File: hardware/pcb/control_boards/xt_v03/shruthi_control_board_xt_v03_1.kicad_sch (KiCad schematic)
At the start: 29 parts, among them IC1 24LC512, IC10 ATMEGA644p, J1 CV, J2 POWER, J3 M03PTH, J4 POWER, Q1 20MHz, U1 AVRISP, X1 MIDI, X2 MIDI

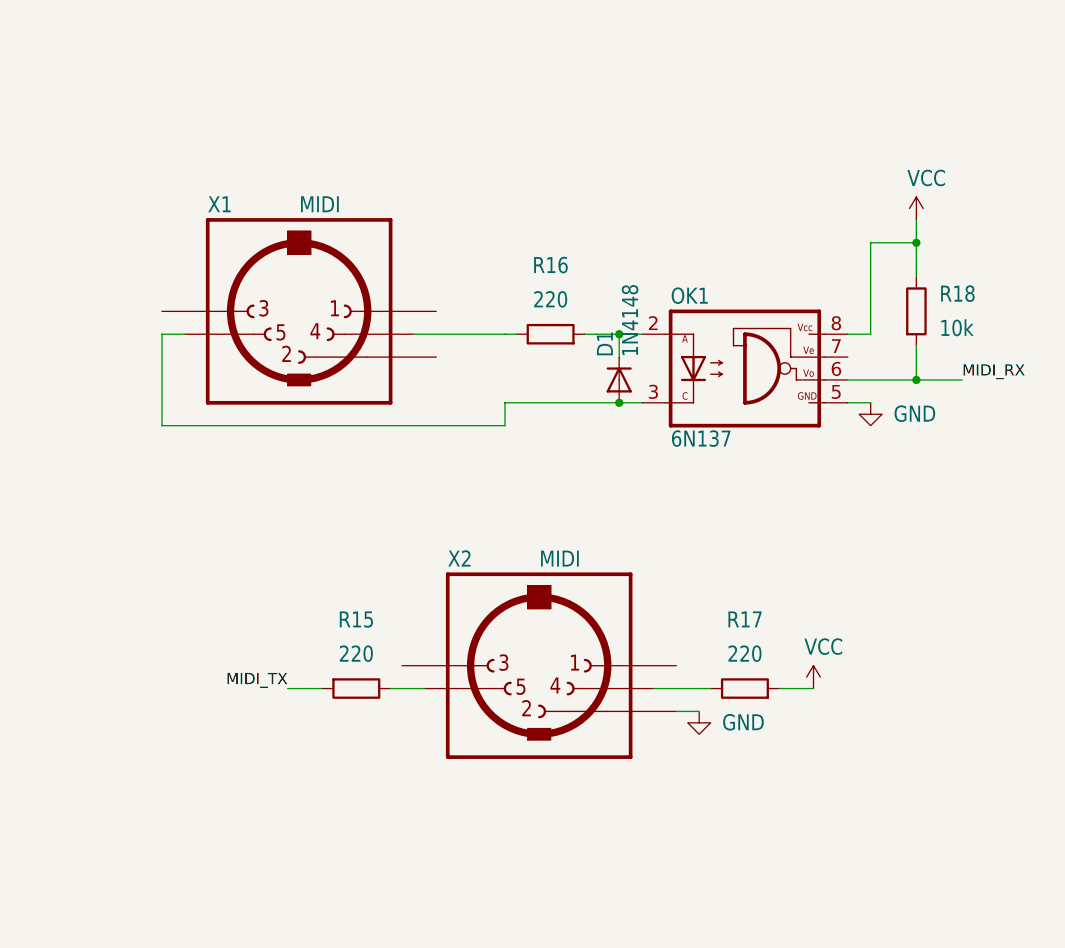
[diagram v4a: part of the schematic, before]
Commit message: update MIDI circuitry to use kicad symbols
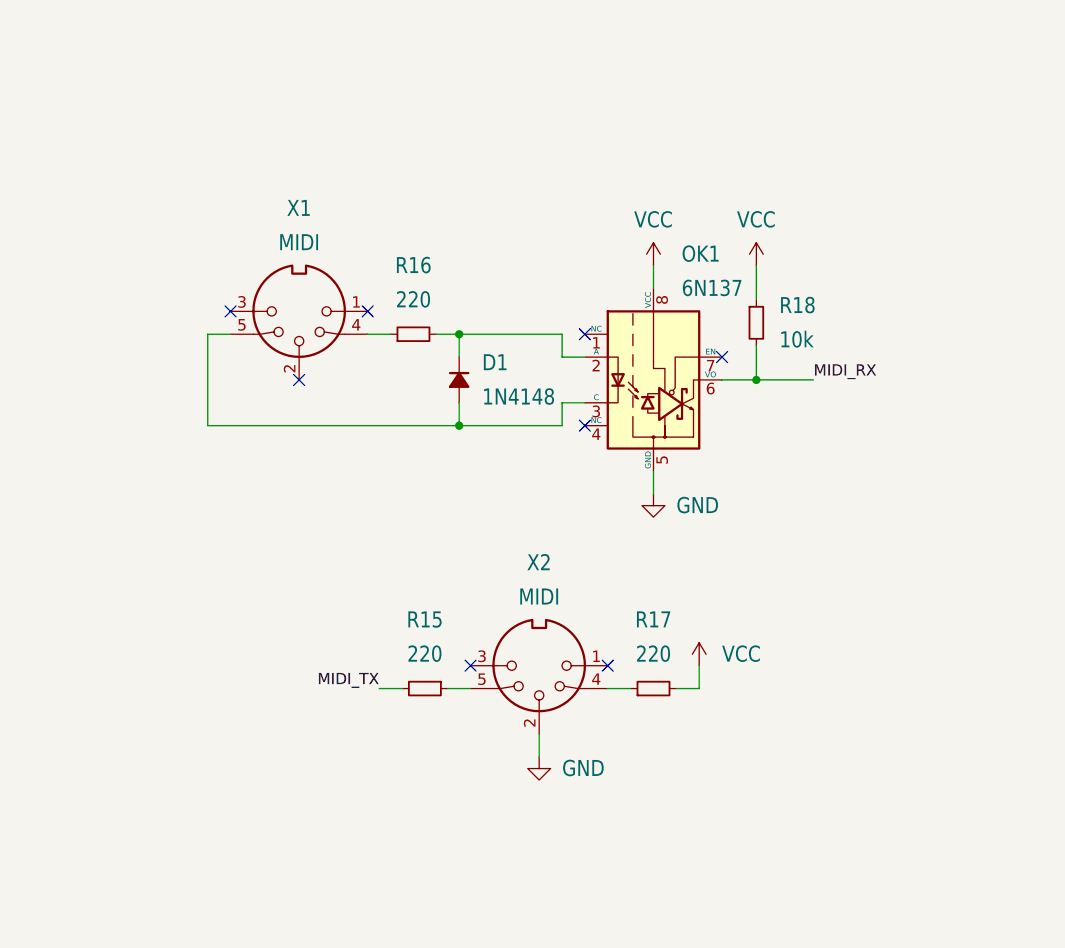
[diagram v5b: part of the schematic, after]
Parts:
- D1: symbol shruthi_control_board_xt_v03-eagle-import:DIODE-D-5 -> Device:D_Small_Filled
- OK1: footprint shruthi_control_board_xt_v03:DIL08 -> Package_DIP:DIP-8_W7.62mm; symbol shruthi_control_board_xt_v03-eagle-import:6N137 -> Isolator:6N137
- R15, R16, R17, R18: symbol Device:R -> Device:R_Small
- X1, X2: symbol shruthi_control_board_xt_v03-eagle-import:MAB5SH -> Connector:DIN-5_180degree
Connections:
- net at OK1.2 (A), R16.2: now also D1.1 (K); no longer D1.C
- net at OK1.3 (C), X1.5: now also D1.2 (A); no longer D1.A
- no-connect marks 0 -> 8
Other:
- moved on the sheet: R15, R16, R17, R18

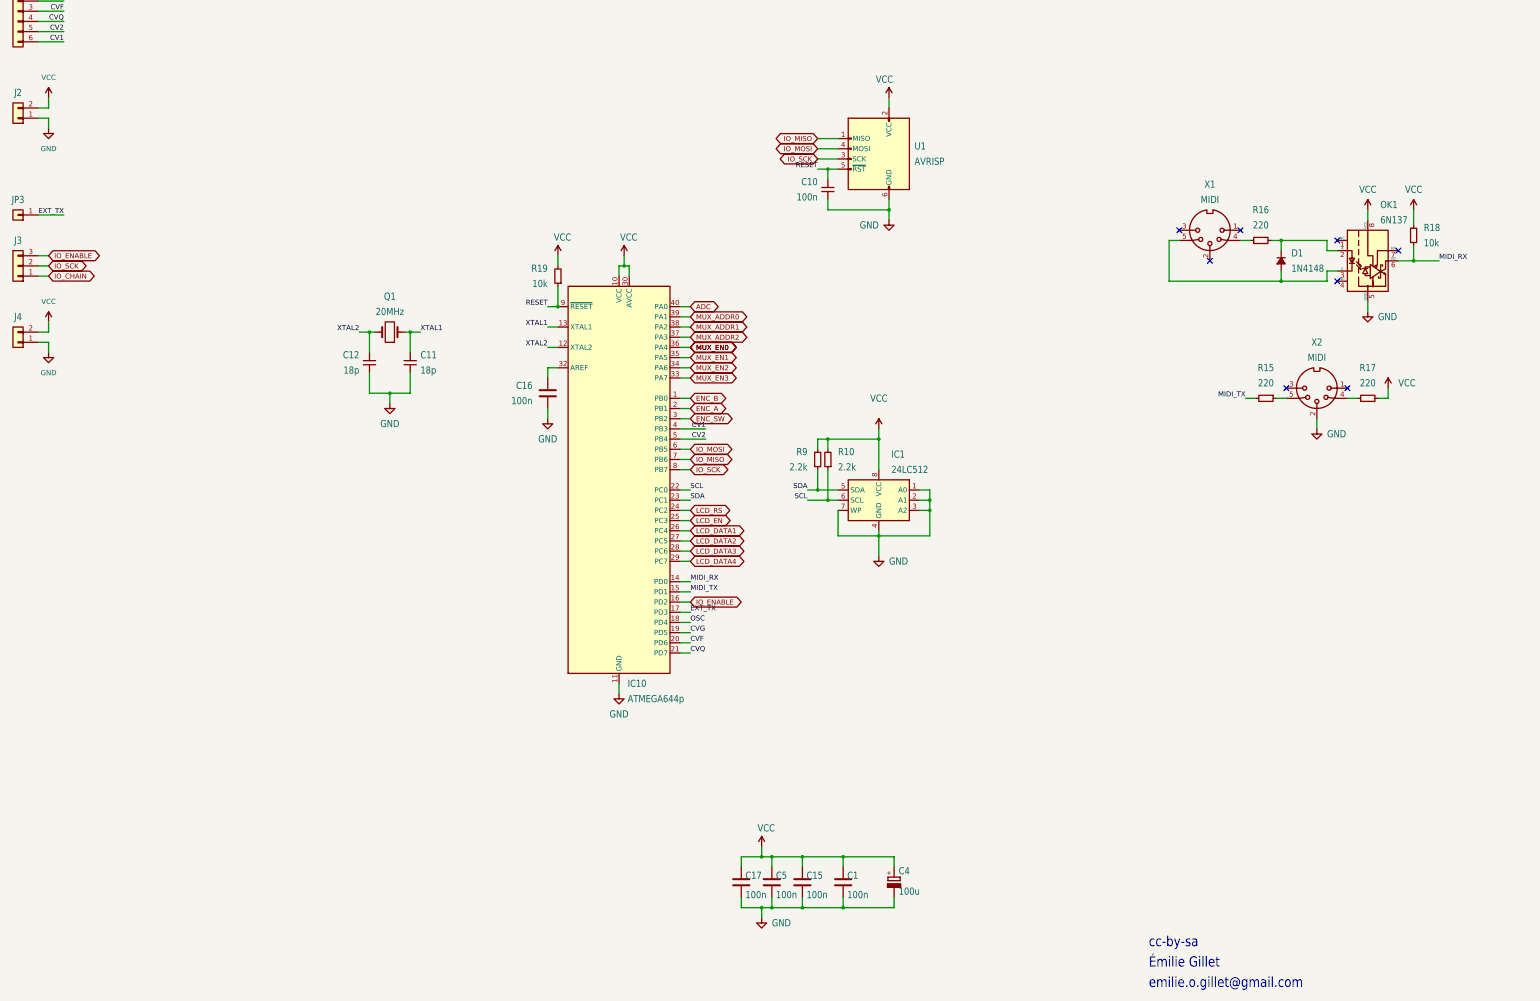
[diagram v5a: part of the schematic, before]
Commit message: move bypass capacitors next to respective devices
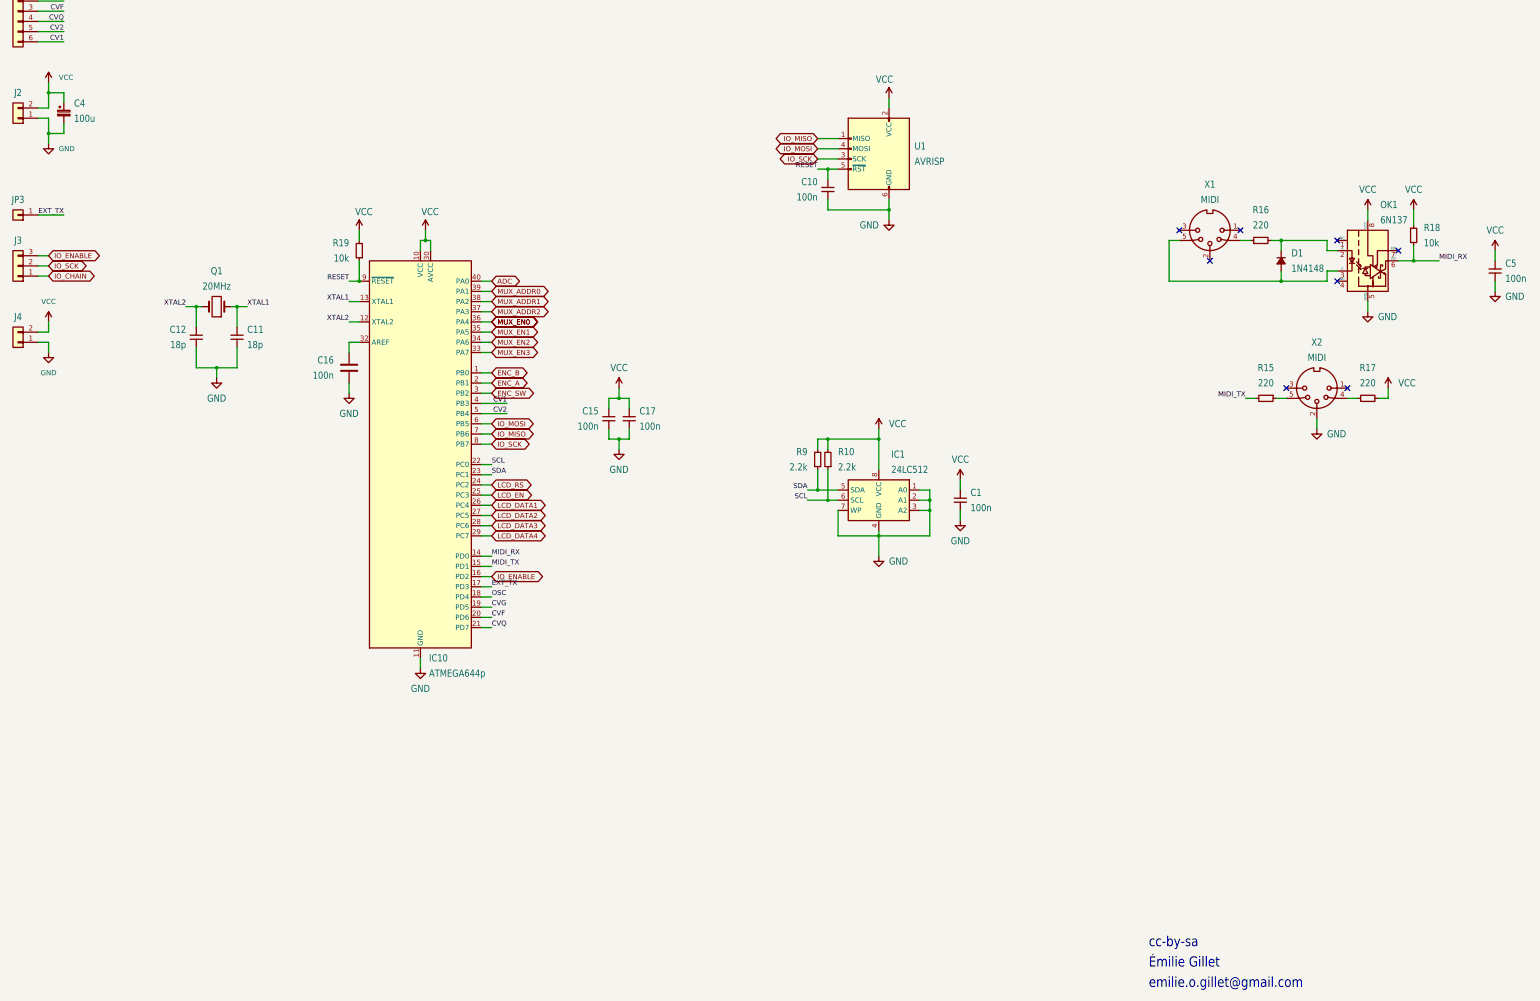
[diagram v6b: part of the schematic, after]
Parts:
- C1, C15, C17, C5: symbol Device:C -> Device:C_Small
- C4: symbol shruthi_control_board_xt_v03-eagle-import:CPOL-EUE2.5-7 -> Device:C_Polarized_Small
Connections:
- net GND: now also C4.2; no longer C4.-
- net VCC: now also C4.1; no longer C4.+
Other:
- moved on the sheet: C1, C11, C12, C15, C16, C17, C5, IC10, Q1, R19

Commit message: update footprints for atmega and 6N137
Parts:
- IC10: footprint Package_DIP:DIP-40_W15.24mm -> Package_DIP:DIP-40_W15.24mm_Socket_LongPads
- OK1: footprint Package_DIP:DIP-8_W7.62mm -> Package_DIP:DIP-8_W7.62mm_Socket_LongPads
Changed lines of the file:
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@@
 			)
 		)
-		(property "Footprint" "Package_DIP:DIP-40_W15.24mm"
+		(property "Footprint" "Package_DIP:DIP-40_W15.24mm_Socket_LongPads"
 			(at 125.73 135.89 0)
 			(effects
@@
 			)
 		)
-		(property "Footprint" "Package_DIP:DIP-8_W7.62mm"
+		(property "Footprint" "Package_DIP:DIP-8_W7.62mm_Socket_LongPads"
 			(at 361.95 100.33 0)
 			(effects

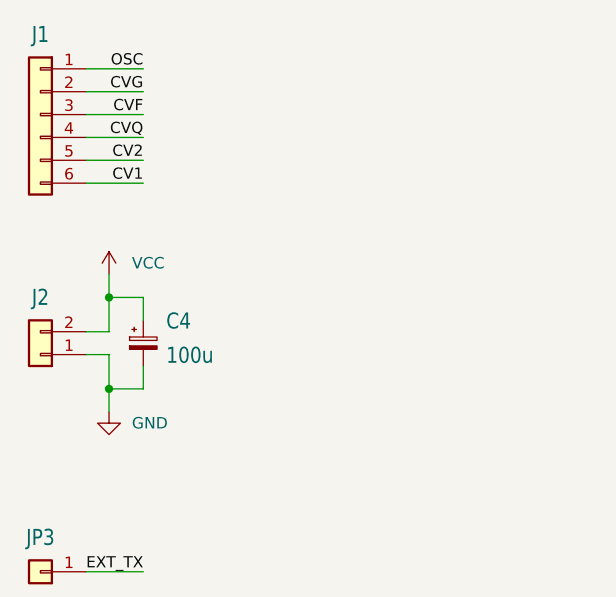
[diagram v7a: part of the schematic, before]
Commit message: use 1x8 header instead of separate ones for J1 and J2
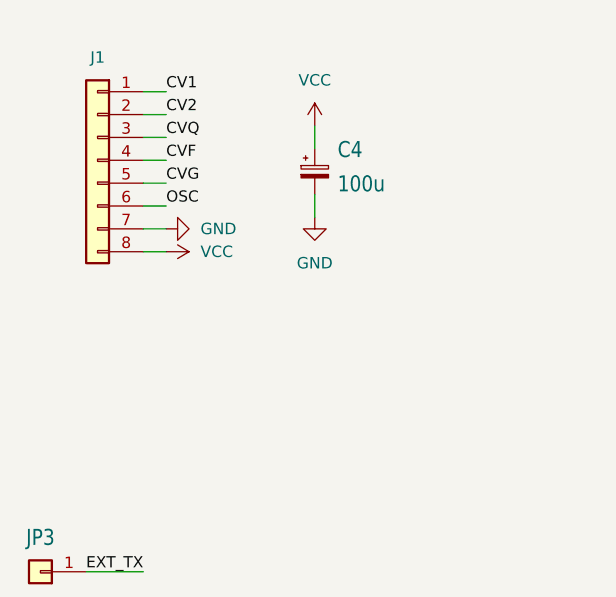
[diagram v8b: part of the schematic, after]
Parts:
- removed J1: CV, shruthi_control_board_xt_v03:1X06, symbol Connector_Generic:Conn_01x06
- removed J2: POWER, shruthi_control_board_xt_v03:1X02, symbol Connector_Generic:Conn_01x02
- added J1: Conn_01x08, Connector_PinHeader_2.54mm:PinHeader_1x08_P2.54mm_Vertical, symbol Connector_Generic:Conn_01x08
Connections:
- net CV1: now also J1.1 (Pin_1)
- net CV2: now also J1.2 (Pin_2)
- net CVF: now also J1.4 (Pin_4)
- net CVG: now also J1.5 (Pin_5)
- net CVQ: now also J1.3 (Pin_3)
- net GND: now also J1.7 (Pin_7)
- net OSC: now also J1.6 (Pin_6)
- net VCC: now also J1.8 (Pin_8)
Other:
- moved on the sheet: C4
